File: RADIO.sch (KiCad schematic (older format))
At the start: 39 parts, among them Q801 BSS138, U801 A7, U802 SIM_SLOT

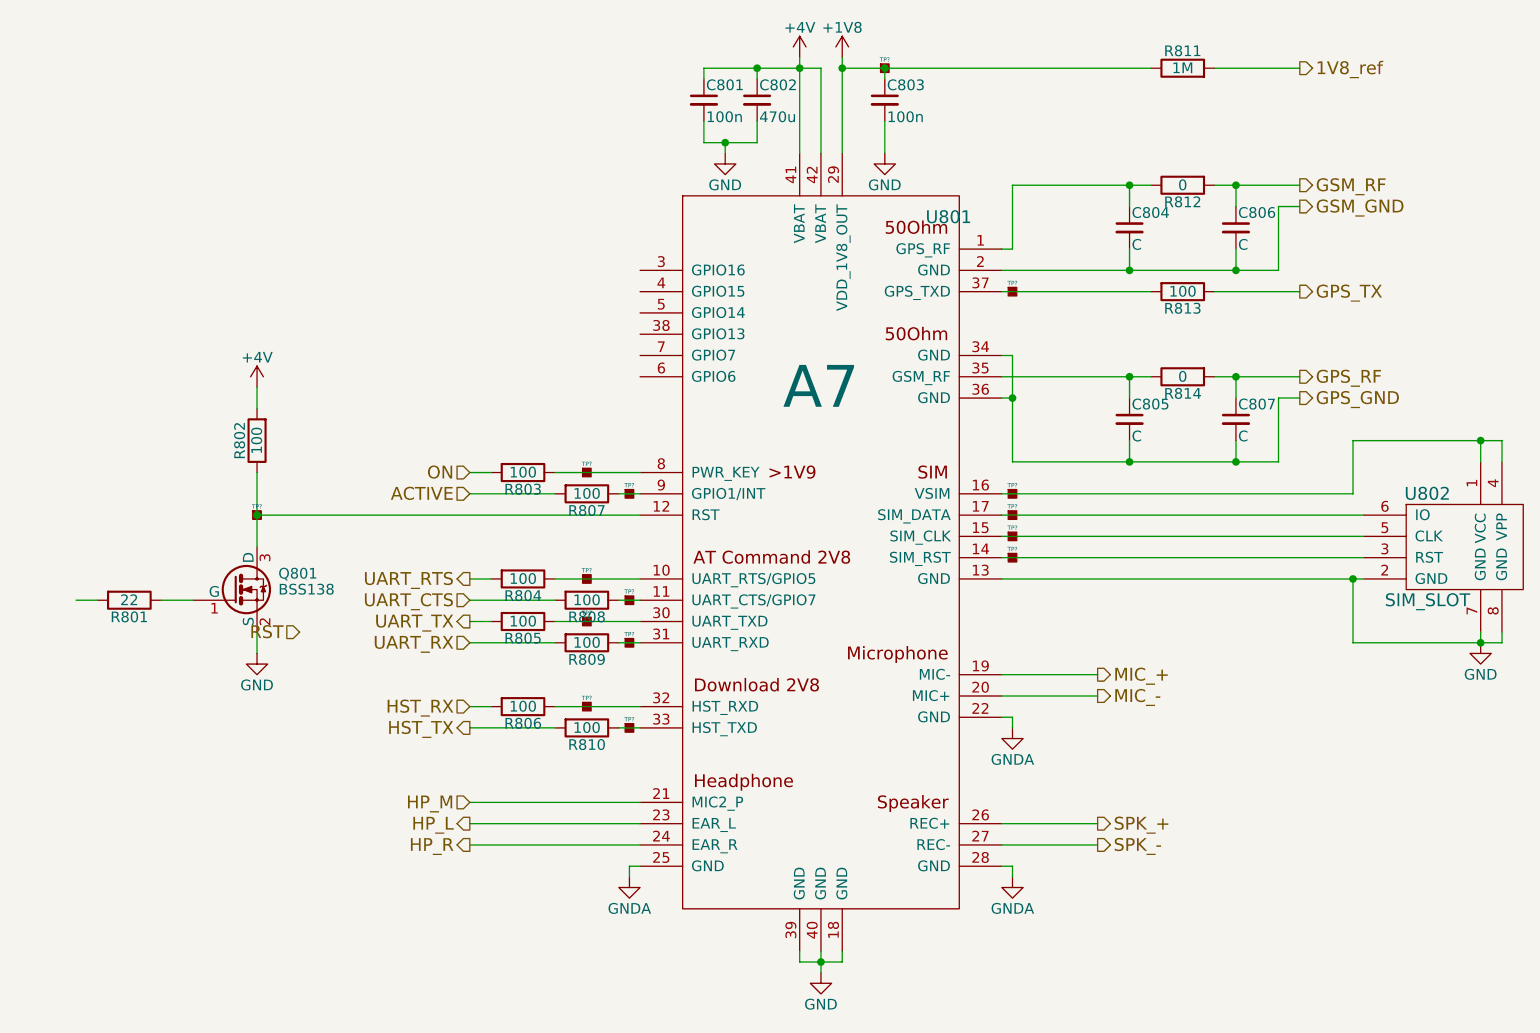
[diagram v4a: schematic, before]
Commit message: moved to some Bus routing for serveral communication signals on the top sheet. This reduces lines on the top sheet.
Changed 4V boost converter circuit toi use TPS61046 for size reasons
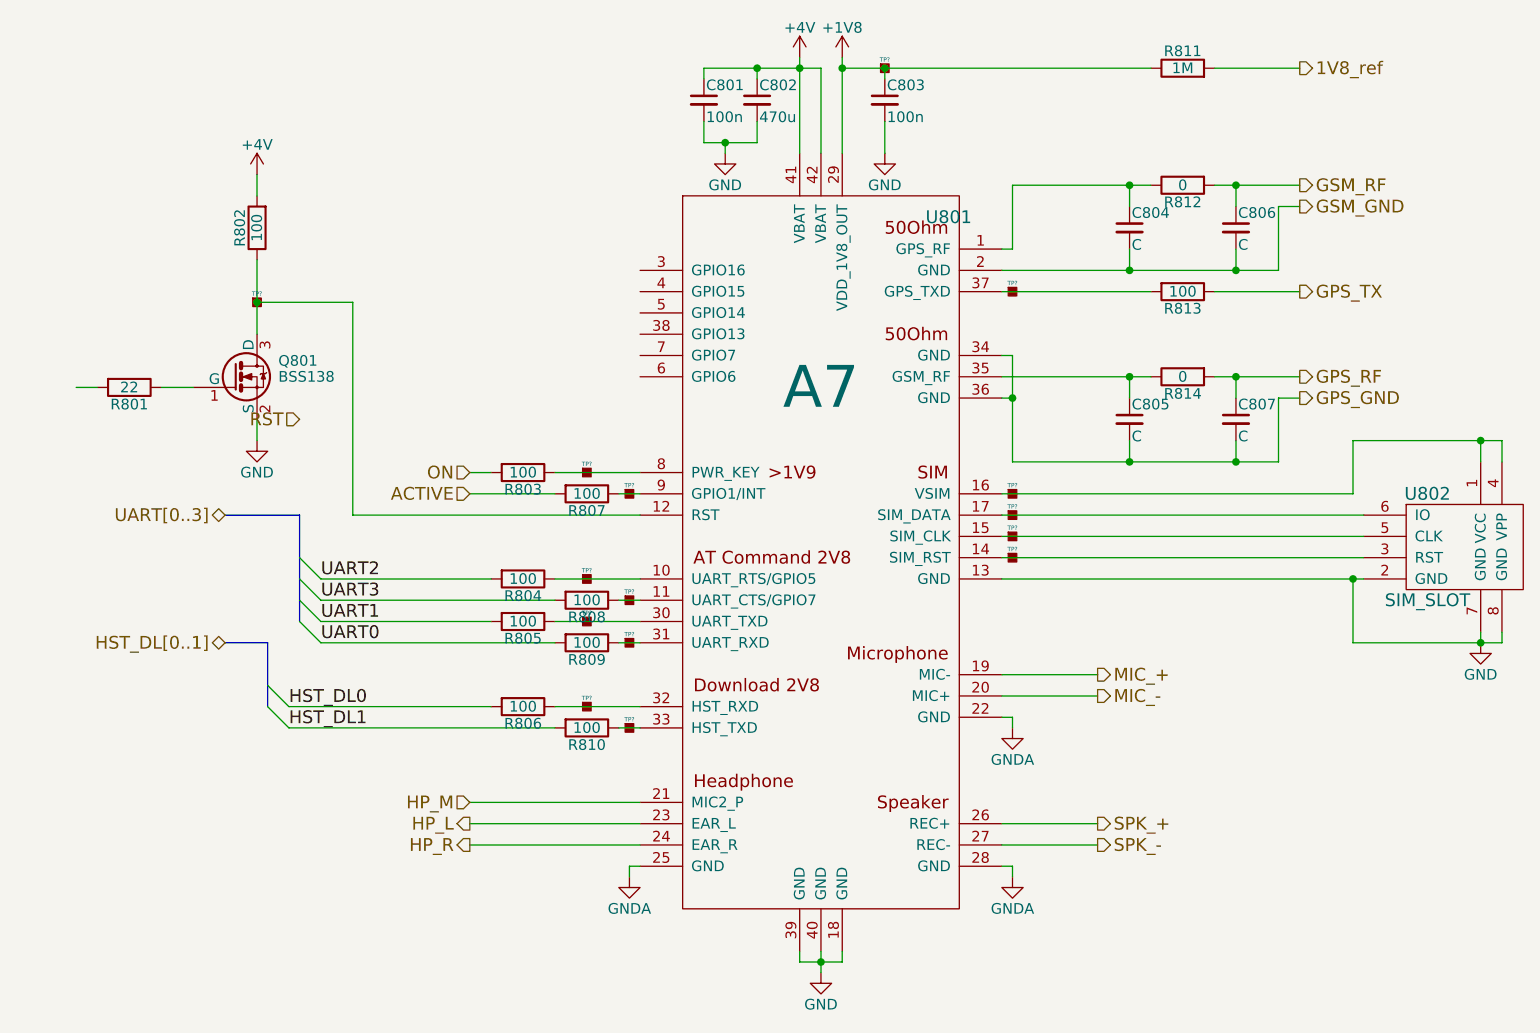
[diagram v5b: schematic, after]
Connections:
- net HST_RX renamed HST_DL0
- net HST_TX renamed HST_DL1
- net UART_CTS renamed UART3
- net UART_RTS renamed UART2
- net UART_RX renamed UART0
- net UART_TX renamed UART1
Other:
- moved on the sheet: Q801, R801, R802, TP?
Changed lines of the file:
@@
 LIBS:tp
 LIBS:w3006
+LIBS:tps61046
 LIBS:3210retro-cache
 EELAYER 25 0
@@
 $Descr A4 11693 8268
 encoding utf-8
-Sheet 6 9
+Sheet 5 9
 Title "Nokia 3210 Retrofit"
-Date "2016-12-20"
+Date "2016-12-22"
 Rev "1"
 Comp "www.kurzschluss-blog.de"
@@
 	1    0    0    -1
 $EndComp
-Text HLabel 3200 3950 0    60   Output ~ 0
-UART_RTS
-Text HLabel 3200 4050 0    60   Input ~ 0
-UART_CTS
-Text HLabel 3200 4150 0    60   Output ~ 0
-UART_TX
-Text HLabel 3200 4250 0    60   Input ~ 0
-UART_RX
-Text HLabel 3200 4550 0    60   Input ~ 0
-HST_RX
-Text HLabel 3200 4650 0    60   Output ~ 0
-HST_TX
 $Comp
 L R R810
@@
 	3600 4550 4000 4550
 Wire Wire Line
-	3600 4650 3200 4650
-Wire Wire Line
-	3300 4550 3200 4550
+	3600 4650 2350 4650
+Wire Wire Line
+	3300 4550 2350 4550
 $Comp
 L R R809
@@
 	4000 4250 3900 4250
 Wire Wire Line
-	3600 4250 3200 4250
-Wire Wire Line
-	3200 4150 3300 4150
+	2500 4250 3600 4250
+Wire Wire Line
+	2500 4150 3300 4150
 Wire Wire Line
 	3600 4150 4000 4150
@@
 	4000 4050 3900 4050
 Wire Wire Line
-	3600 4050 3200 4050
-Wire Wire Line
-	3200 3950 3300 3950
+	2500 4050 3600 4050
+Wire Wire Line
+	2500 3950 3300 3950
 Text HLabel 3200 3450 0    60   Input ~ 0
 ON
@@
 L BSS138 Q801
 U 1 1 5805F82C
-P 2100 4000
-F 0 "Q801" H 2300 4075 50  0000 L CNN
-F 1 "BSS138" H 2300 4000 50  0000 L CNN
-F 2 "TO_SOT_Packages_SMD:SOT-23" H 2300 3925 50  0001 L CIN
-F 3 "" H 2100 4000 50  0000 L CNN
-	1    2100 4000
-	1    0    0    -1
-$EndComp
-Wire Wire Line
-	4000 3650 2200 3650
-Wire Wire Line
-	2200 3450 2200 3800
+P 2100 3000
+F 0 "Q801" H 2300 3075 50  0000 L CNN
+F 1 "BSS138" H 2300 3000 50  0000 L CNN
+F 2 "TO_SOT_Packages_SMD:SOT-23" H 2300 2925 50  0001 L CIN
+F 3 "" H 2100 3000 50  0000 L CNN
+	1    2100 3000
+	1    0    0    -1
+$EndComp
+Wire Wire Line
+	2650 2650 2200 2650
+Wire Wire Line
+	2200 2450 2200 2650
+Wire Wire Line
+	2200 2650 2200 2800
 $Comp
 L R R807
@@
 L GND #PWR602
 U 1 1 5805FAC7
-P 2200 4300
-F 0 "#PWR602" H 2200 4050 50  0001 C CNN
-F 1 "GND" H 2200 4150 50  0000 C CNN
-F 2 "" H 2200 4300 50  0000 C CNN
-F 3 "" H 2200 4300 50  0000 C CNN
-	1    2200 4300
-	1    0    0    -1
-$EndComp
-Wire Wire Line
-	2200 4300 2200 4200
+P 2200 3300
+F 0 "#PWR602" H 2200 3050 50  0001 C CNN
+F 1 "GND" H 2200 3150 50  0000 C CNN
+F 2 "" H 2200 3300 50  0000 C CNN
+F 3 "" H 2200 3300 50  0000 C CNN
+	1    2200 3300
+	1    0    0    -1
+$EndComp
+Wire Wire Line
+	2200 3300 2200 3200
 $Comp
 L R R801
 U 1 1 5805FB29
-P 1600 4050
-F 0 "R801" V 1680 4050 50  0000 C CNN
-F 1 "22" V 1600 4050 50  0000 C CNN
-F 2 "" V 1530 4050 50  0001 C CNN
-F 3 "" H 1600 4050 50  0000 C CNN
-	1    1600 4050
-	0    1    1    0
-$EndComp
-Wire Wire Line
-	1750 4050 1900 4050
-Text HLabel 2400 4200 0    60   Input ~ 0
+P 1600 3050
+F 0 "R801" V 1680 3050 50  0000 C CNN
+F 1 "22" V 1600 3050 50  0000 C CNN
+F 2 "" V 1530 3050 50  0001 C CNN
+F 3 "" H 1600 3050 50  0000 C CNN
+	1    1600 3050
+	0    1    1    0
+$EndComp
+Wire Wire Line
+	1750 3050 1900 3050
+Text HLabel 2400 3200 0    60   Input ~ 0
 RST
 Wire Wire Line
-	1350 4050 1450 4050
+	1350 3050 1450 3050
 $Comp
 L R R802
 U 1 1 5805FDA3
-P 2200 3300
-F 0 "R802" V 2280 3300 50  0000 C CNN
-F 1 "100" V 2200 3300 50  0000 C CNN
-F 2 "" V 2130 3300 50  0001 C CNN
-F 3 "" H 2200 3300 50  0000 C CNN
-	1    2200 3300
+P 2200 2300
+F 0 "R802" V 2280 2300 50  0000 C CNN
+F 1 "100" V 2200 2300 50  0000 C CNN
+F 2 "" V 2130 2300 50  0001 C CNN
+F 3 "" H 2200 2300 50  0000 C CNN
+	1    2200 2300
 	-1   0    0    1
 $EndComp
-Connection ~ 2200 3650
-Wire Wire Line
-	2200 3050 2200 3150
+Connection ~ 2200 2650
+Wire Wire Line
+	2200 2050 2200 2150
 $Comp
 L +4V #PWR601
 U 1 1 5805FFE4
-P 2200 3050
-F 0 "#PWR601" H 2200 2900 50  0001 C CNN
-F 1 "+4V" H 2200 3190 50  0000 C CNN
-F 2 "" H 2200 3050 50  0000 C CNN
-F 3 "" H 2200 3050 50  0000 C CNN
-	1    2200 3050
+P 2200 2050
+F 0 "#PWR601" H 2200 1900 50  0001 C CNN
+F 1 "+4V" H 2200 2190 50  0000 C CNN
+F 2 "" H 2200 2050 50  0000 C CNN
+F 3 "" H 2200 2050 50  0000 C CNN
+	1    2200 2050
 	1    0    0    -1
 $EndComp
@@
 	6800 3100 6800 3000
 Wire Wire Line
-	6700 3000 7100 3000
+	6700 3000 6800 3000
+Wire Wire Line
+	6800 3000 7100 3000
 Connection ~ 6800 3000
 Wire Wire Line
-	5700 3000 6400 3000
+	5700 3000 6300 3000
+Wire Wire Line
+	6300 3000 6400 3000
 Wire Wire Line
 	6300 3000 6300 3100
@@
 	7000 3400 7000 3100
 Wire Wire Line
-	5750 3400 7000 3400
-Wire Wire Line
-	5750 2900 5750 3400
+	5750 3400 6300 3400
+Wire Wire Line
+	6300 3400 6800 3400
+Wire Wire Line
+	6800 3400 7000 3400
+Wire Wire Line
+	5750 2900 5750 3100
+Wire Wire Line
+	5750 3100 5750 3400
 Wire Wire Line
 	5750 3100 5700 3100
@@
 	6800 2200 6800 2100
 Wire Wire Line
-	6700 2100 7100 2100
+	6700 2100 6800 2100
+Wire Wire Line
+	6800 2100 7100 2100
 Connection ~ 6800 2100
 Wire Wire Line
-	5750 2100 6400 2100
+	5750 2100 6300 2100
+Wire Wire Line
+	6300 2100 6400 2100
 Wire Wire Line
 	6300 2100 6300 2200
@@
 	7000 2500 7000 2200
 Wire Wire Line
-	5700 2500 7000 2500
+	5700 2500 6300 2500
+Wire Wire Line
+	6300 2500 6800 2500
+Wire Wire Line
+	6800 2500 7000 2500
 Wire Wire Line
 	6300 2400 6300 2500
@@
 $EndComp
 Wire Wire Line
-	4850 5700 4850 5800
+	4850 5700 4850 5750
+Wire Wire Line
+	4850 5750 4850 5800
 Wire Wire Line
 	4750 5700 4750 5750
 Wire Wire Line
-	4750 5750 4950 5750
+	4750 5750 4850 5750
+Wire Wire Line
+	4850 5750 4950 5750
 Connection ~ 4850 5750
 Wire Wire Line
@@
 $EndComp
 Wire Wire Line
-	4750 1500 4750 1950
+	4750 1500 4750 1550
+Wire Wire Line
+	4750 1550 4750 1950
 Wire Wire Line
 	4850 1550 4850 1950
 Wire Wire Line
-	4300 1550 4850 1550
+	4300 1550 4550 1550
+Wire Wire Line
+	4550 1550 4750 1550
+Wire Wire Line
+	4750 1550 4850 1550
 Connection ~ 4750 1550
 Wire Wire Line
@@
 	4550 1900 4550 1800
 Wire Wire Line
-	4300 1900 4550 1900
+	4300 1900 4400 1900
+Wire Wire Line
+	4400 1900 4550 1900
 Wire Wire Line
 	4300 1800 4300 1900
@@
 $EndComp
 Wire Wire Line
-	5700 3950 7400 3950
+	5700 3950 7350 3950
+Wire Wire Line
+	7350 3950 7400 3950
 Wire Wire Line
 	5700 3850 7400 3850
@@
 	7350 3550 7350 3300
 Wire Wire Line
-	7350 3300 8050 3300
+	7350 3300 7950 3300
+Wire Wire Line
+	7950 3300 8050 3300
 Wire Wire Line
 	7950 3300 7950 3400
@@
 	7950 4200 7950 4250
 Wire Wire Line
-	7350 4250 8050 4250
+	7350 4250 7950 4250
+Wire Wire Line
+	7950 4250 8050 4250
 Wire Wire Line
 	7350 4250 7350 3950
@@
 $EndComp
 Wire Wire Line
-	4950 1500 4950 1950
+	4950 1500 4950 1550
+Wire Wire Line
+	4950 1550 4950 1950
 $Comp
 L C_Small C803
@@
 Connection ~ 5150 1550
 Wire Wire Line
-	4950 1550 6400 1550
+	4950 1550 5150 1550
+Wire Wire Line
+	5150 1550 6400 1550
 Wire Wire Line
 	6700 1550 7100 1550
@@
 L TP TP?
 U 1 1 585B8948
-P 2200 3650
-F 0 "TP?" H 2200 3690 20  0000 C CNN
-F 1 "TP" H 2200 3600 60  0001 C CNN
-F 2 "" H 2200 3650 60  0000 C CNN
-F 3 "" H 2200 3650 60  0000 C CNN
-	1    2200 3650
+P 2200 2650
+F 0 "TP?" H 2200 2690 20  0000 C CNN
+F 1 "TP" H 2200 2600 60  0001 C CNN
+F 2 "" H 2200 2650 60  0000 C CNN
+F 3 "" H 2200 2650 60  0000 C CNN
+	1    2200 2650
 	1    0    0    -1
 $EndComp
@@
 	1    0    0    -1
 $EndComp
+Wire Wire Line
+	2650 2650 2650 3650
+Wire Wire Line
+	2650 3650 4000 3650
+Text HLabel 2050 3650 0    60   BiDi ~ 0
+UART[0..3]
+Entry Wire Line
+	2400 3850 2500 3950
+Entry Wire Line
+	2400 4150 2500 4250
+Entry Wire Line
+	2400 4050 2500 4150
+Entry Wire Line
+	2400 3950 2500 4050
+Wire Bus Line
+	2400 3650 2400 3850
+Wire Bus Line
+	2400 3850 2400 3950
+Wire Bus Line
+	2400 3950 2400 4050
+Wire Bus Line
+	2400 4050 2400 4150
+Wire Bus Line
+	2400 3650 2050 3650
+Text Label 2500 3950 0    60   ~ 0
+UART2
+Text Label 2500 4050 0    60   ~ 0
+UART3
+Text Label 2500 4150 0    60   ~ 0
+UART1
+Text Label 2500 4250 0    60   ~ 0
+UART0
+Entry Wire Line
+	2250 4550 2350 4650
+Entry Wire Line
+	2250 4450 2350 4550
+Text Label 2350 4550 0    60   ~ 0
+HST_DL0
+Text Label 2350 4650 0    60   ~ 0
+HST_DL1
+Wire Bus Line
+	2250 4550 2250 4450
+Wire Bus Line
+	2250 4450 2250 4250
+Wire Bus Line
+	2250 4250 2050 4250
+Text HLabel 2050 4250 0    60   BiDi ~ 0
+HST_DL[0..1]
 $EndSCHEMATC

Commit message: aktuelle Version
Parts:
- C801, C802, C803, C804, C805, C806, C807: footprint (none) -> Capacitors_SMD:C_0603
- R801, R802, R803, R804, R805, R806, R807, R808, R809, R810, R811, R812, R813, R814: footprint (none) -> Resistors_SMD:R_0603
- TP501, TP502, TP503, TP504, TP505, TP506, TP507, TP508, TP509, TP510, TP511, TP512, TP513, TP514, TP515: renamed from TP?; footprint (none) -> buttons:TP

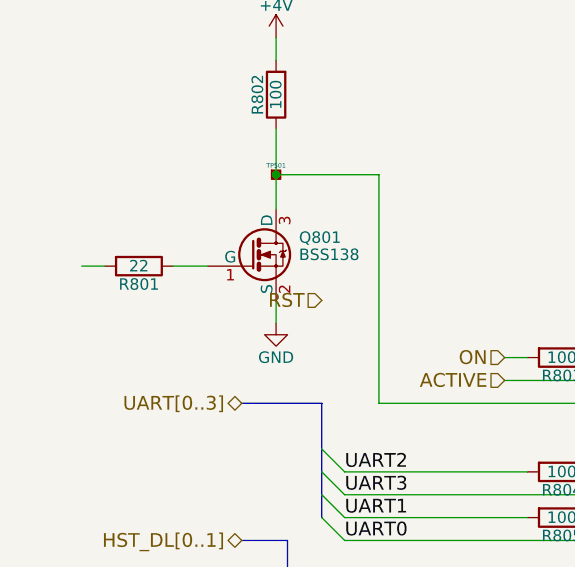
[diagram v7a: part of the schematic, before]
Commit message: added some audio circuitry
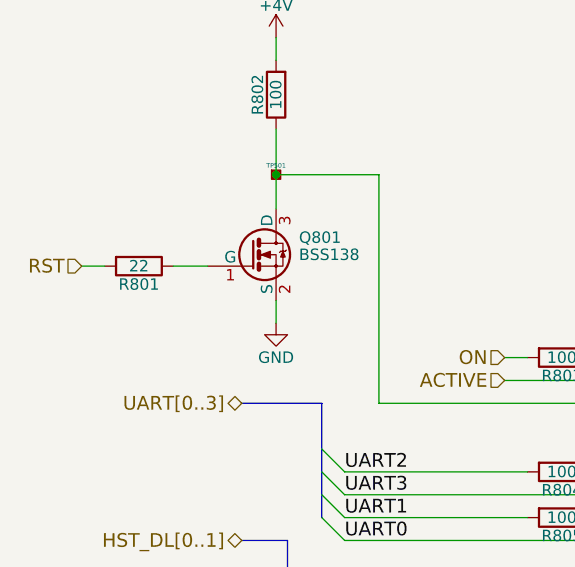
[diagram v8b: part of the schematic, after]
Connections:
- net RST: now also R801.2
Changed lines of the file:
@@
 LIBS:w3006
 LIBS:tps61046
+LIBS:mp34dt01tr
+LIBS:drv8601
+LIBS:lm4930
+LIBS:ts5a22366
 LIBS:3210retro-cache
 EELAYER 25 0
@@
 Wire Wire Line
 	1750 3050 1900 3050
-Text HLabel 2400 3200 0    60   Input ~ 0
+Text HLabel 1350 3050 0    60   Input ~ 0
 RST
 Wire Wire Line
